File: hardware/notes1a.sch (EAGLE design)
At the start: 4 parts, among them U1 LMP7721, U2 MAX4477

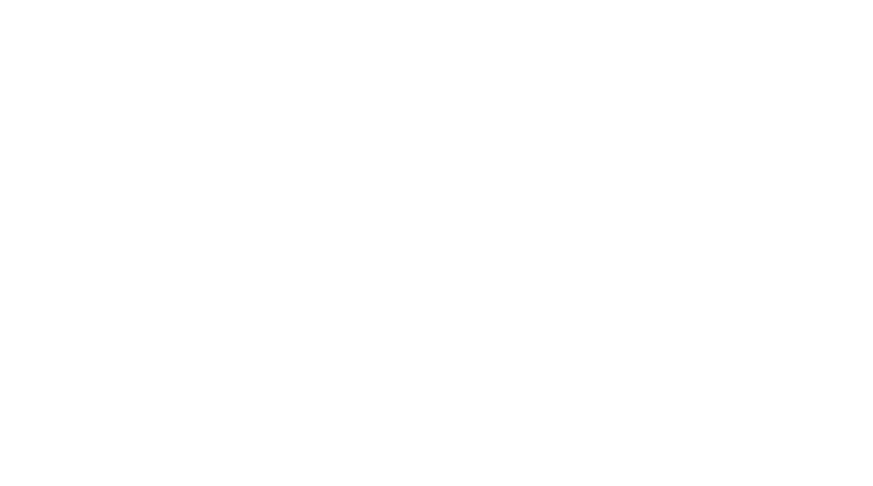
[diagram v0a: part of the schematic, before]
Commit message: Added PIC microcontroller
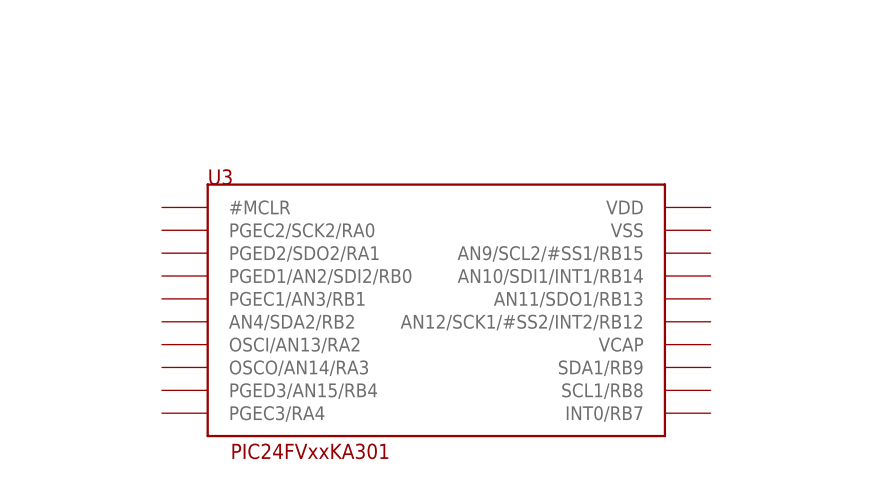
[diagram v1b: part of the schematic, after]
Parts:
- added U3: PIC24FVXXKA301, openct:PIC24FVXXKA301
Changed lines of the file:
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@@
 <part name="U2" library="openct" deviceset="OPAMP-MAX4477" device="" value="MAX4477"/>
 <part name="U$1" library="openct" deviceset="1X06" device=""/>
+<part name="U3" library="openct" deviceset="PIC24FVXXKA301" device=""/>
 </parts>
 <sheets>
@@
 <instance part="U2" gate="B" x="93.98" y="-2.54"/>
 <instance part="U$1" gate="G$1" x="-22.86" y="-38.1"/>
+<instance part="U3" gate="G$1" x="35.56" y="-88.9"/>
 </instances>
 <busses>

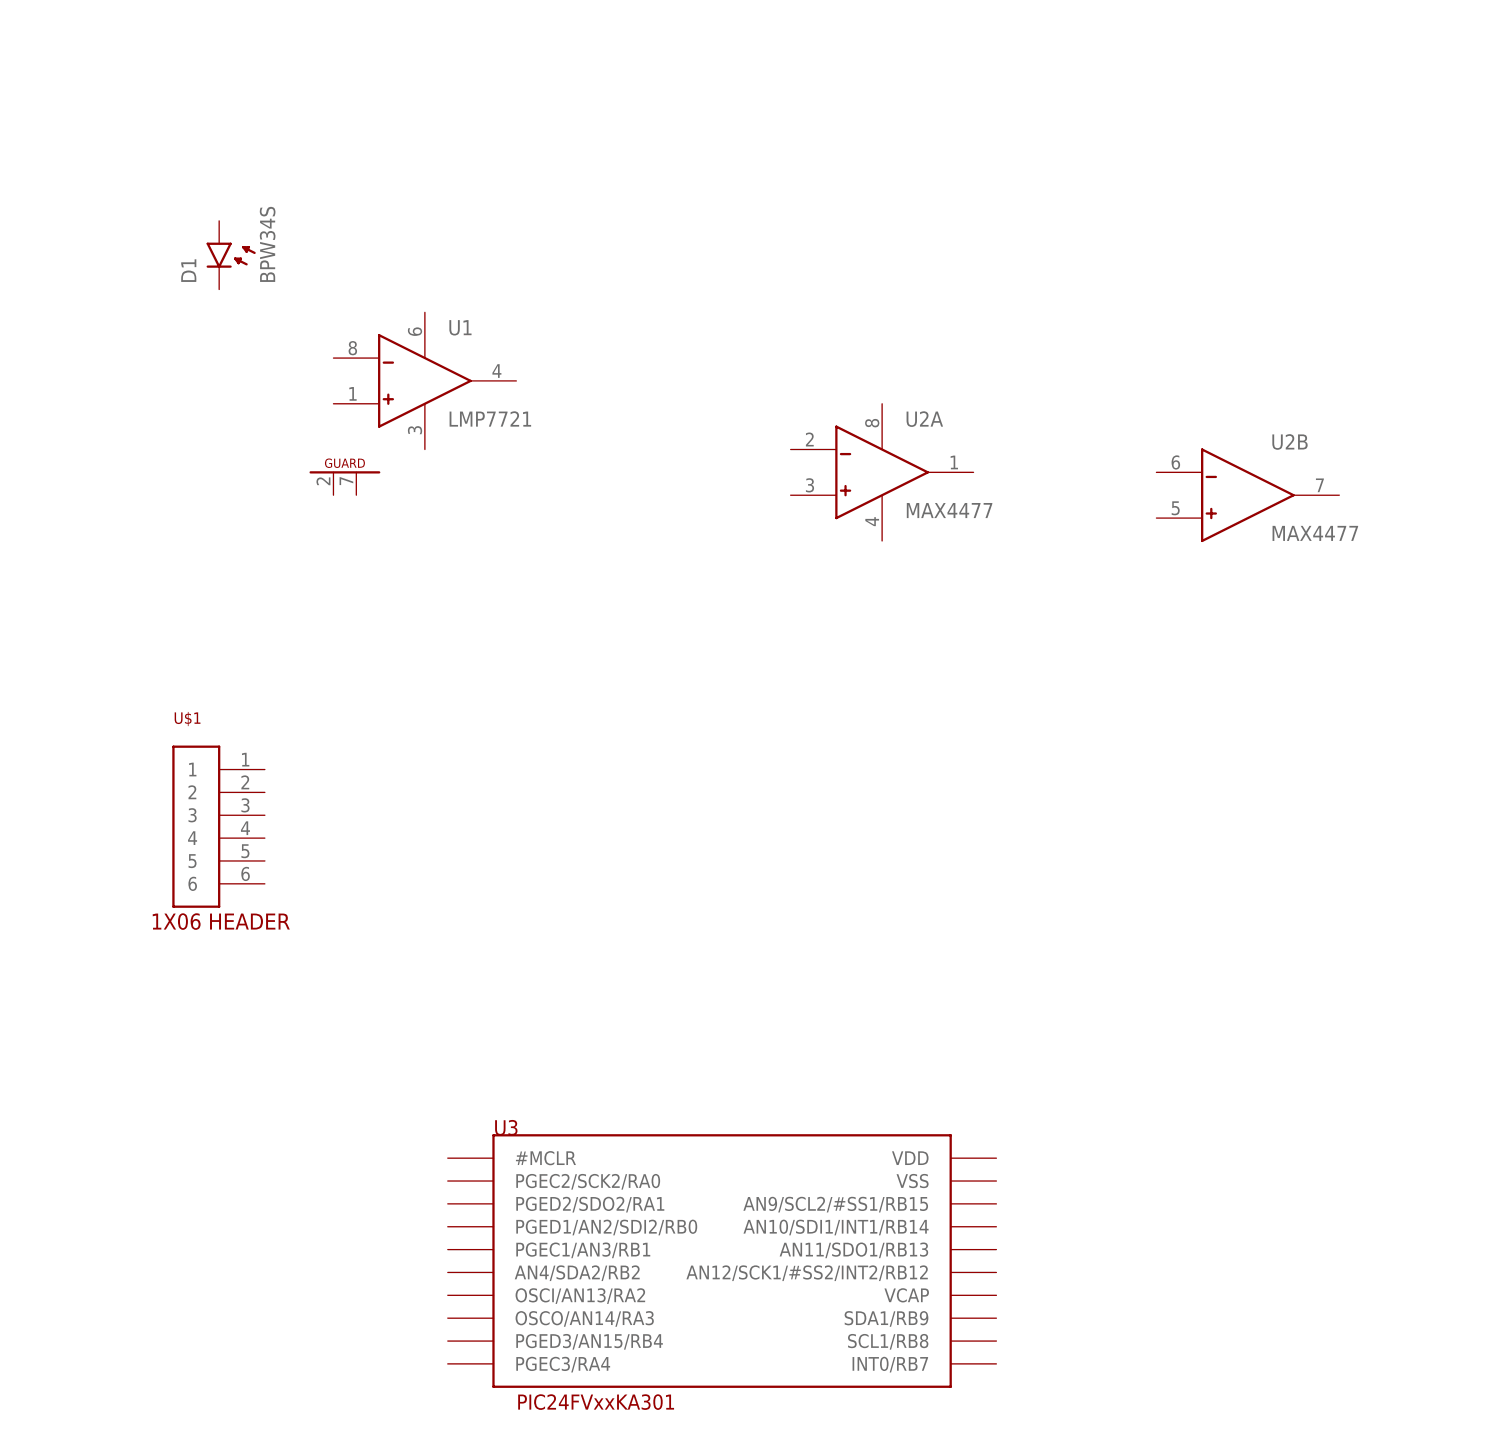
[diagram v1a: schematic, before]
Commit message: Added photodiode preamplifier
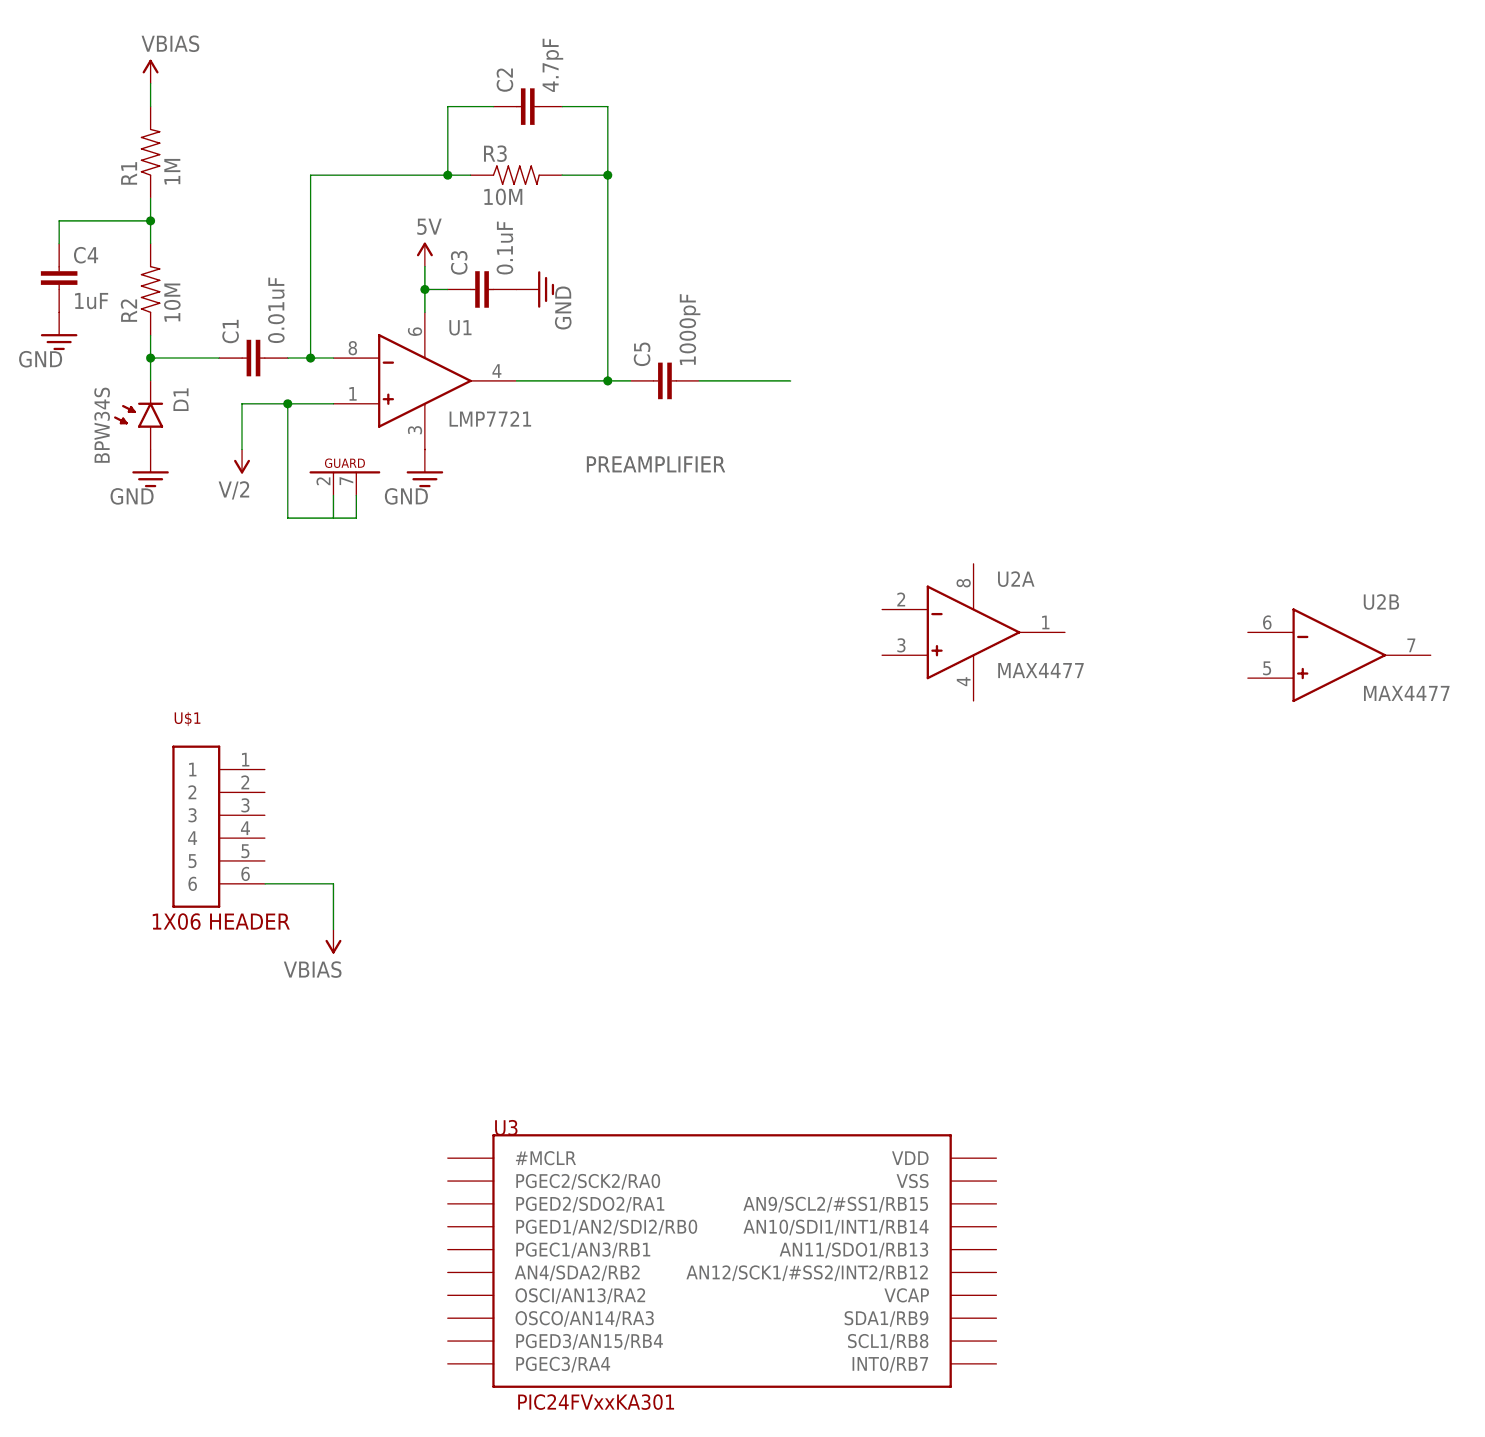
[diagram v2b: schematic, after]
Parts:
- added C1: 0.01uF, openct:CAP0603
- added C2: 4.7pF, openct:CAP0603
- added C3: 0.1uF, openct:CAP0603
- added C4: 1uF, openct:CAP0603
- added C5: 1000pF, openct:CAP0603
- added R1: 1M, openct:RESISTOR0603
- added R2, R3: 10M, openct:RESISTOR0603
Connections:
- new net 5V: C3.1, U1.VCC
- new net GND: C3.2, C4.2, D1.ANODE, U1.GND
- new net N$1: C1.2, C2.1, R3.1, U1.-
- new net N$10: C5.2
- new net N$2: C1.1, D1.CATHODE, R2.1
- new net N$4: C4.1, R1.1, R2.2
- new net N$7: C2.2, C5.1, R3.2, U1.OUT
- new net V/2: U1.+, U1.G1, U1.G2
- new net VBIAS: R1.2, U$1.6
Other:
- note added: "PREAMPLIFIER"
- moved on the sheet: D1, U2A, U2B
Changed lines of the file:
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@@
 <part name="U$1" library="openct" deviceset="1X06" device=""/>
 <part name="U3" library="openct" deviceset="PIC24FVXXKA301" device=""/>
+<part name="C1" library="openct" deviceset="CAP" device="0603" value="0.01uF"/>
+<part name="C2" library="openct" deviceset="CAP" device="0603" value="4.7pF"/>
+<part name="C3" library="openct" deviceset="CAP" device="0603" value="0.1uF"/>
+<part name="C4" library="openct" deviceset="CAP" device="0603" value="1uF"/>
+<part name="R1" library="openct" deviceset="RESISTOR" device="0603" value="1M"/>
+<part name="R2" library="openct" deviceset="RESISTOR" device="0603" value="10M"/>
+<part name="R3" library="openct" deviceset="RESISTOR" device="0603" value="10M"/>
+<part name="C5" library="openct" deviceset="CAP" device="0603" value="1000pF"/>
+<part name="GND1" library="openct" deviceset="GND" device=""/>
+<part name="GND2" library="openct" deviceset="GND" device=""/>
+<part name="GND3" library="openct" deviceset="GND" device=""/>
+<part name="GND4" library="openct" deviceset="GND" device=""/>
+<part name="U$2" library="openct" deviceset="5V" device=""/>
+<part name="U$3" library="openct" deviceset="V/2" device=""/>
+<part name="U$4" library="openct" deviceset="VBIAS" device=""/>
+<part name="U$6" library="openct" deviceset="VBIAS" device=""/>
 </parts>
 <sheets>
 <sheet>
 <plain>
+<text x="20.32" y="0" size="1.778" layer="97">PREAMPLIFIER</text>
 </plain>
 <instances>
-<instance part="D1" gate="G$1" x="-20.32" y="25.4"/>
+<instance part="D1" gate="G$1" x="-27.94" y="5.08" rot="R180"/>
 <instance part="U1" gate="G$1" x="2.54" y="10.16"/>
-<instance part="U2" gate="A" x="53.34" y="0"/>
-<instance part="U2" gate="B" x="93.98" y="-2.54"/>
+<instance part="U2" gate="A" x="63.5" y="-17.78"/>
+<instance part="U2" gate="B" x="104.14" y="-20.32"/>
 <instance part="U$1" gate="G$1" x="-22.86" y="-38.1"/>
 <instance part="U3" gate="G$1" x="35.56" y="-88.9"/>
+<instance part="C1" gate="G$1" x="-15.24" y="12.7" rot="R90"/>
+<instance part="C2" gate="G$1" x="15.24" y="40.64" rot="R90"/>
+<instance part="C3" gate="G$1" x="10.16" y="20.32" rot="R90"/>
+<instance part="C4" gate="G$1" x="-38.1" y="20.32"/>
+<instance part="R1" gate="G$1" x="-27.94" y="35.56" rot="R90"/>
+<instance part="R2" gate="G$1" x="-27.94" y="20.32" rot="R90"/>
+<instance part="R3" gate="G$1" x="12.7" y="33.02"/>
+<instance part="C5" gate="G$1" x="30.48" y="10.16" rot="R90"/>
+<instance part="GND1" gate="1" x="-27.94" y="0"/>
+<instance part="GND2" gate="1" x="-38.1" y="15.24"/>
+<instance part="GND3" gate="1" x="15.24" y="20.32" rot="R90"/>
+<instance part="GND4" gate="1" x="2.54" y="0"/>
+<instance part="U$2" gate="G$1" x="2.54" y="22.86"/>
+<instance part="U$3" gate="G$1" x="-17.78" y="2.54" rot="R180"/>
+<instance part="U$4" gate="G$1" x="-27.94" y="43.18"/>
+<instance part="U$6" gate="G$1" x="-7.62" y="-50.8" rot="R180"/>
 </instances>
 <busses>
 </busses>
 <nets>
+<net name="N$1" class="0">
+<segment>
+<pinref part="U1" gate="G$1" pin="-"/>
+<pinref part="C1" gate="G$1" pin="2"/>
+<wire x1="-7.62" y1="12.7" x2="-10.16" y2="12.7" width="0.1524" layer="91"/>
+<wire x1="-10.16" y1="12.7" x2="-12.7" y2="12.7" width="0.1524" layer="91"/>
+<wire x1="-10.16" y1="12.7" x2="-10.16" y2="33.02" width="0.1524" layer="91"/>
+<pinref part="R3" gate="G$1" pin="1"/>
+<wire x1="-10.16" y1="33.02" x2="5.08" y2="33.02" width="0.1524" layer="91"/>
+<junction x="-10.16" y="12.7"/>
+<pinref part="C2" gate="G$1" pin="1"/>
+<wire x1="5.08" y1="33.02" x2="7.62" y2="33.02" width="0.1524" layer="91"/>
+<wire x1="10.16" y1="40.64" x2="5.08" y2="40.64" width="0.1524" layer="91"/>
+<wire x1="5.08" y1="40.64" x2="5.08" y2="33.02" width="0.1524" layer="91"/>
+<junction x="5.08" y="33.02"/>
+</segment>
+</net>
+<net name="N$2" class="0">
+<segment>
+<pinref part="C1" gate="G$1" pin="1"/>
+<wire x1="-20.32" y1="12.7" x2="-27.94" y2="12.7" width="0.1524" layer="91"/>
+<pinref part="D1" gate="G$1" pin="CATHODE"/>
+<pinref part="R2" gate="G$1" pin="1"/>
+<wire x1="-27.94" y1="10.16" x2="-27.94" y2="12.7" width="0.1524" layer="91"/>
+<junction x="-27.94" y="12.7"/>
+<wire x1="-27.94" y1="12.7" x2="-27.94" y2="15.24" width="0.1524" layer="91"/>
+</segment>
+</net>
+<net name="N$4" class="0">
+<segment>
+<pinref part="R2" gate="G$1" pin="2"/>
+<pinref part="R1" gate="G$1" pin="1"/>
+<wire x1="-27.94" y1="25.4" x2="-27.94" y2="27.94" width="0.1524" layer="91"/>
+<wire x1="-27.94" y1="27.94" x2="-27.94" y2="30.48" width="0.1524" layer="91"/>
+<wire x1="-27.94" y1="27.94" x2="-38.1" y2="27.94" width="0.1524" layer="91"/>
+<pinref part="C4" gate="G$1" pin="1"/>
+<wire x1="-38.1" y1="27.94" x2="-38.1" y2="25.4" width="0.1524" layer="91"/>
+<junction x="-27.94" y="27.94"/>
+</segment>
+</net>
+<net name="N$7" class="0">
+<segment>
+<pinref part="U1" gate="G$1" pin="OUT"/>
+<pinref part="C5" gate="G$1" pin="1"/>
+<wire x1="12.7" y1="10.16" x2="22.86" y2="10.16" width="0.1524" layer="91"/>
+<pinref part="R3" gate="G$1" pin="2"/>
+<wire x1="22.86" y1="10.16" x2="25.4" y2="10.16" width="0.1524" layer="91"/>
+<wire x1="17.78" y1="33.02" x2="22.86" y2="33.02" width="0.1524" layer="91"/>
+<wire x1="22.86" y1="33.02" x2="22.86" y2="10.16" width="0.1524" layer="91"/>
+<pinref part="C2" gate="G$1" pin="2"/>
+<wire x1="17.78" y1="40.64" x2="22.86" y2="40.64" width="0.1524" layer="91"/>
+<wire x1="22.86" y1="40.64" x2="22.86" y2="33.02" width="0.1524" layer="91"/>
+<junction x="22.86" y="33.02"/>
+<junction x="22.86" y="10.16"/>
+</segment>
+</net>
+<net name="GND" class="0">
+<segment>
+<pinref part="D1" gate="G$1" pin="ANODE"/>
+<pinref part="GND1" gate="1" pin="GND"/>
+</segment>
+<segment>
+<pinref part="C4" gate="G$1" pin="2"/>
+<pinref part="GND2" gate="1" pin="GND"/>
+</segment>
+<segment>
+<pinref part="C3" gate="G$1" pin="2"/>
+<pinref part="GND3" gate="1" pin="GND"/>
+</segment>
+<segment>
+<pinref part="U1" gate="G$1" pin="GND"/>
+<pinref part="GND4" gate="1" pin="GND"/>
+</segment>
+</net>
+<net name="5V" class="0">
+<segment>
+<pinref part="U1" gate="G$1" pin="VCC"/>
+<wire x1="2.54" y1="17.78" x2="2.54" y2="20.32" width="0.1524" layer="91"/>
+<pinref part="C3" gate="G$1" pin="1"/>
+<wire x1="2.54" y1="20.32" x2="2.54" y2="22.86" width="0.1524" layer="91"/>
+<wire x1="5.08" y1="20.32" x2="2.54" y2="20.32" width="0.1524" layer="91"/>
+<junction x="2.54" y="20.32"/>
+<pinref part="U$2" gate="G$1" pin="5V"/>
+</segment>
+</net>
+<net name="N$10" class="0">
+<segment>
+<pinref part="C5" gate="G$1" pin="2"/>
+<wire x1="33.02" y1="10.16" x2="43.18" y2="10.16" width="0.1524" layer="91"/>
+</segment>
+</net>
+<net name="V/2" class="0">
+<segment>
+<pinref part="U1" gate="G$1" pin="+"/>
+<wire x1="-7.62" y1="7.62" x2="-12.7" y2="7.62" width="0.1524" layer="91"/>
+<pinref part="U1" gate="G$1" pin="G2"/>
+<wire x1="-12.7" y1="7.62" x2="-17.78" y2="7.62" width="0.1524" layer="91"/>
+<wire x1="-5.08" y1="-2.54" x2="-5.08" y2="-5.08" width="0.1524" layer="91"/>
+<wire x1="-5.08" y1="-5.08" x2="-7.62" y2="-5.08" width="0.1524" layer="91"/>
+<wire x1="-7.62" y1="-5.08" x2="-12.7" y2="-5.08" width="0.1524" layer="91"/>
+<wire x1="-12.7" y1="-5.08" x2="-12.7" y2="7.62" width="0.1524" layer="91"/>
+<pinref part="U1" gate="G$1" pin="G1"/>
+<wire x1="-7.62" y1="-2.54" x2="-7.62" y2="-5.08" width="0.1524" layer="91"/>
+<junction x="-12.7" y="7.62"/>
+<pinref part="U$3" gate="G$1" pin="V/2"/>
+<wire x1="-17.78" y1="7.62" x2="-17.78" y2="2.54" width="0.1524" layer="91"/>
+</segment>
+</net>
+<net name="VBIAS" class="0">
+<segment>
+<pinref part="R1" gate="G$1" pin="2"/>
+<wire x1="-27.94" y1="40.64" x2="-27.94" y2="43.18" width="0.1524" layer="91"/>
+<pinref part="U$4" gate="G$1" pin="VBIAS"/>
+</segment>
+<segment>
+<pinref part="U$1" gate="G$1" pin="6"/>
+<wire x1="-15.24" y1="-45.72" x2="-7.62" y2="-45.72" width="0.1524" layer="91"/>
+<wire x1="-7.62" y1="-45.72" x2="-7.62" y2="-50.8" width="0.1524" layer="91"/>
+<pinref part="U$6" gate="G$1" pin="VBIAS"/>
+</segment>
+</net>
 </nets>
 </sheet>
